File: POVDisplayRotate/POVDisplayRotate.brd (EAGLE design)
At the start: 54 x 82 mm, 45 parts, among them U1 STP08DP05, U2 STP08DP05, U3 MPQ4420Q, U5 CY8CKIT-142, U6 M95M01

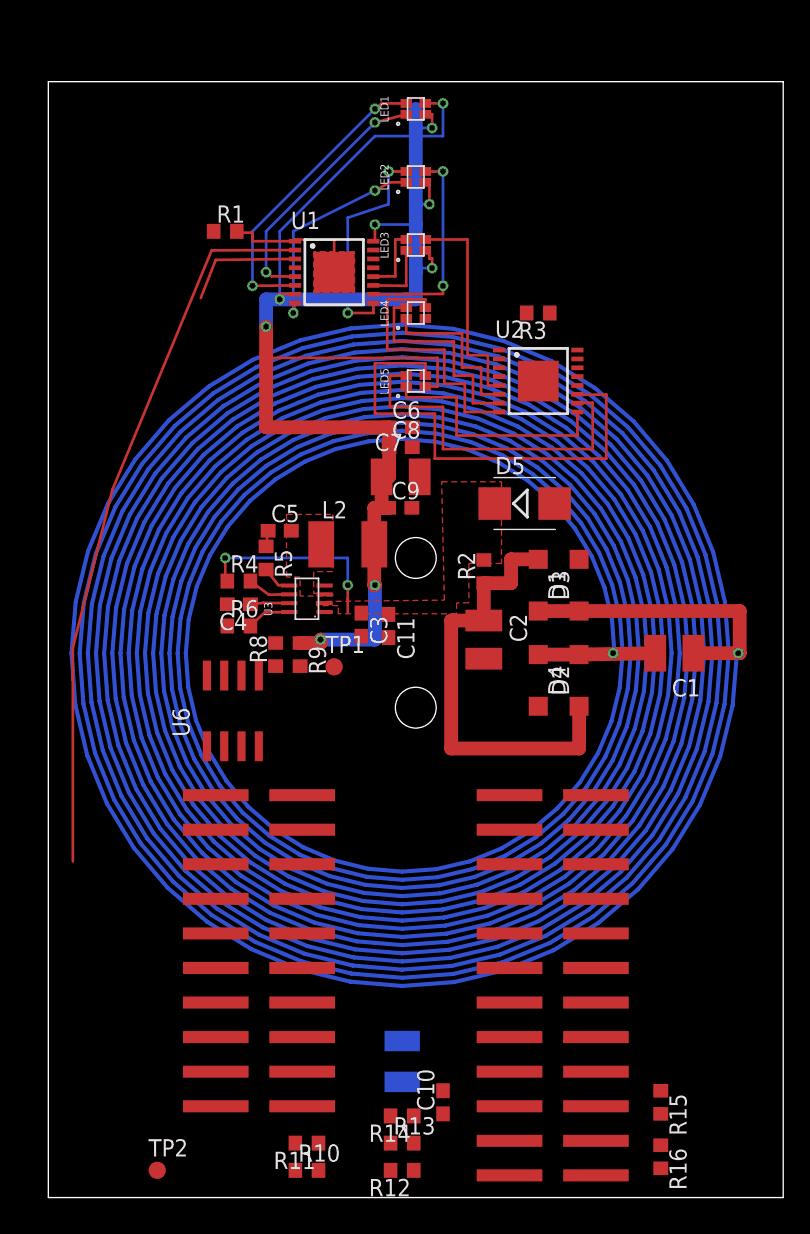
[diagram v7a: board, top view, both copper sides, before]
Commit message: Added additional datasheets and digikey part numbers.
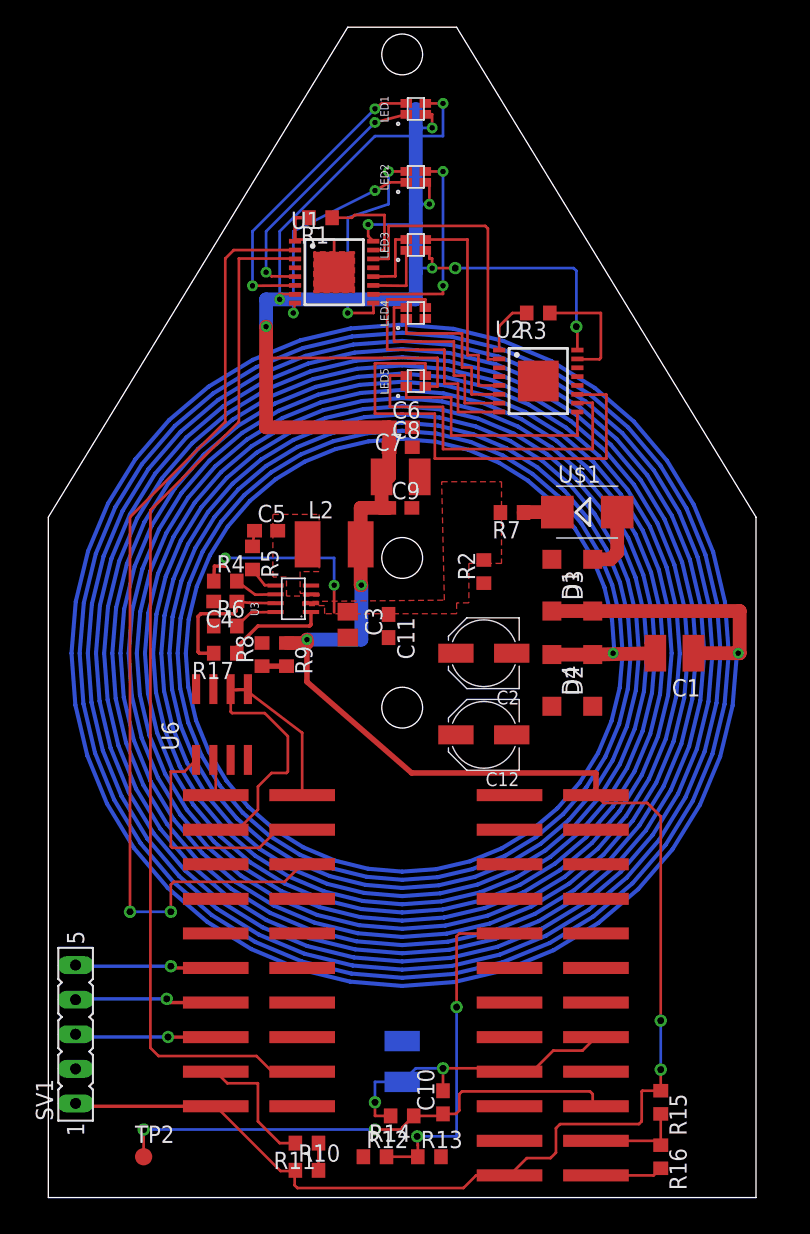
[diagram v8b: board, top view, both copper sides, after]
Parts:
- removed D5: (no value), diode:SMB
- removed TP1: TPB1,27, testpad:B1,27
- added C12: 22u, resistor:PANASONIC_C
- added R17: 100k, resistor:R0603
- added R7: 120, resistor:R0603
- added SV1: (no value), con-lsta:FE05-1
- added U$1: TVS, NicksParts:SMB
- C2: value 1000u -> 22u; device resistor:C1210 -> resistor:PANASONIC_C
- C3: device resistor:C0603 -> resistor:C0805
- R4: value 120 -> 1M
- R8: value 12k -> 7.68k
- moved R1 7.07 mm to (20.0, 72.0), turned to 180 degrees
- moved R12 2.24 mm to (24.0, 3.00), turned to 0 degrees
- moved R13 2.24 mm to (28.0, 3.00)
- moved TP2 1.41 mm to (7.00, 3.00)
- moved U6 1.28 mm to (12.8, 34.8)
- moved C4 1.02 mm to (13.0, 43.8)
- moved C2 1.00 mm to (32.0, 40.0), turned to 180 degrees
- moved C3 1.00 mm to (22.0, 42.1)
- moved C5 1.00 mm to (16.0, 49.0)
- moved D1 1.00 mm to (40.0, 45.0)
- moved D2 1.00 mm to (37.0, 38.0)
- moved D3 1.00 mm to (37.0, 45.0)
- moved D4 1.00 mm to (40.0, 38.0)
- moved L2 1.00 mm to (21.0, 48.0)
- moved R4 1.00 mm to (13.0, 45.3)
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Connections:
- removed net N$16: C2.1, D3.C, D4.C, R2.1
- new net N$11: R7.1, U$1.C
- new net SWDCLK: SV1.4, U5.0.7
- new net SWDIO: SV1.5, U5.0.6
- new net XRES: SV1.3, U5.XRES
- net AGND: now also C12.-, C2.-, U$1.A; no longer C2.2, D5.A
- net GND: now also SV1.2
- net N$1: now also R17.2
- net N$13: now also R17.1; no longer TP1.TP
- net N$3: now also C12.+, C2.+, D3.C, D4.C, R2.1; no longer U5.1.6
- net V+: now also R7.2; no longer D5.C
- net VCC: now also SV1.1
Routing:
- net VCC: track 95.9 -> 219.7 mm, vias 7 -> 11
- net SCLK: track 8.83 -> 76.7 mm
- net OPAMP1_OUT: track 0.00 -> 38.0 mm, vias 0 -> 2
- net N$16: track 32.8 -> 0.00 mm
- net IN_PWR: track 0.00 -> 25.4 mm, vias 0 -> 2
- net OPAMP1_NEG: track 0.00 -> 23.8 mm, vias 0 -> 2
- net AGND: track 10.4 -> 31.8 mm
- net N$18: track 0.00 -> 21.4 mm
- net SDI: track 52.8 -> 71.6 mm, vias 0 -> 2
- net EE_CS: track 0.00 -> 18.0 mm
- net EE_SCLK: track 0.00 -> 17.3 mm
- net EE_MOSI: track 0.00 -> 11.5 mm
- net SWDCLK: track 0.00 -> 10.4 mm, vias 0 -> 1
- net XRES: track 0.00 -> 10.4 mm, vias 0 -> 1
- net SWDIO: track 0.00 -> 10.4 mm, vias 0 -> 1
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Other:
- board size 54 x 82 mm -> 52 x 86 mm
